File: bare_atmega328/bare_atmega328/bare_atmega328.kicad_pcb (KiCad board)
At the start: 2 copper layers, 43.7 x 56.4 mm, 21 parts, among them J1 22-23-2021, J2 22-23-2021, J3 640456-3, J4 22-23-2021, J5 Conn_01x14_Male, J6 Conn_01x14_Male, J7 22-23-2021, SW1 SW_Push, U1 ATMEGA328-PU, U2 NE555DR, Y1 Crystal

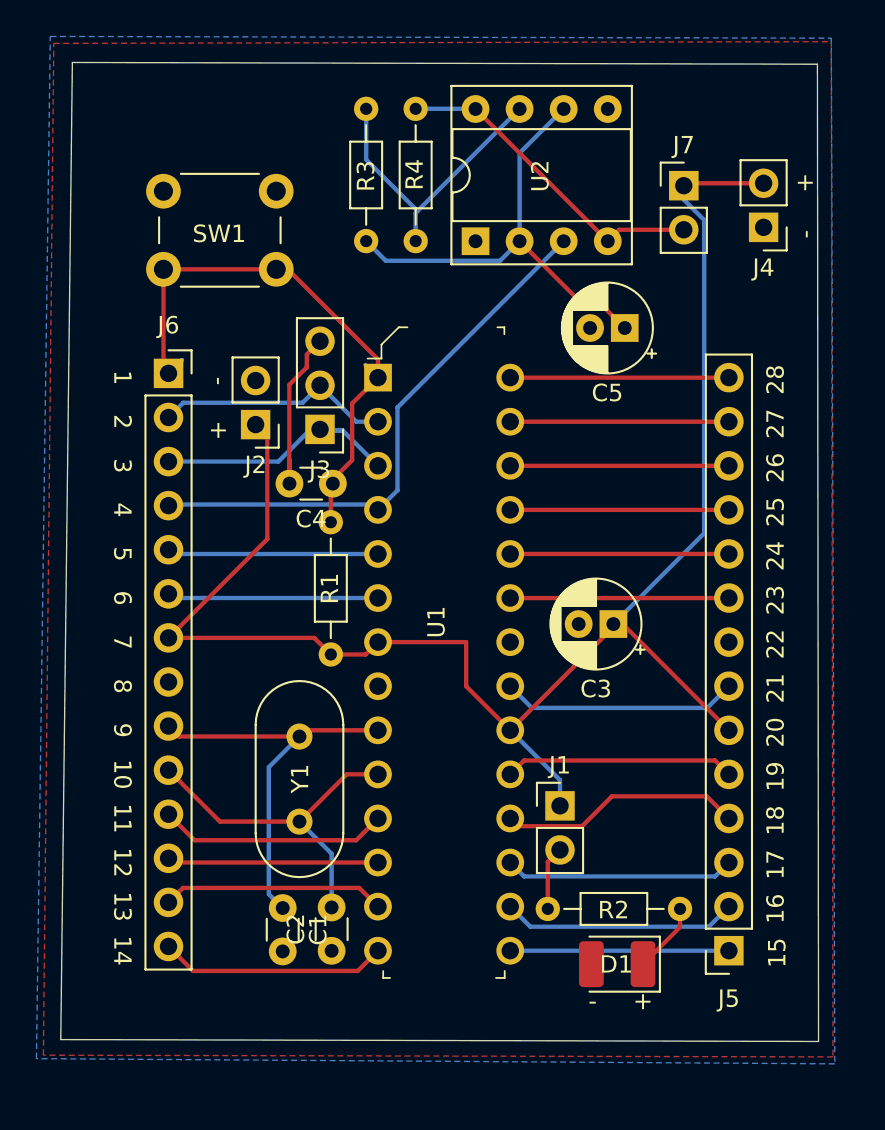
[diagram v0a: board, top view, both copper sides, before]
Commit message: Version v1.2 atmega328 + 555 timer
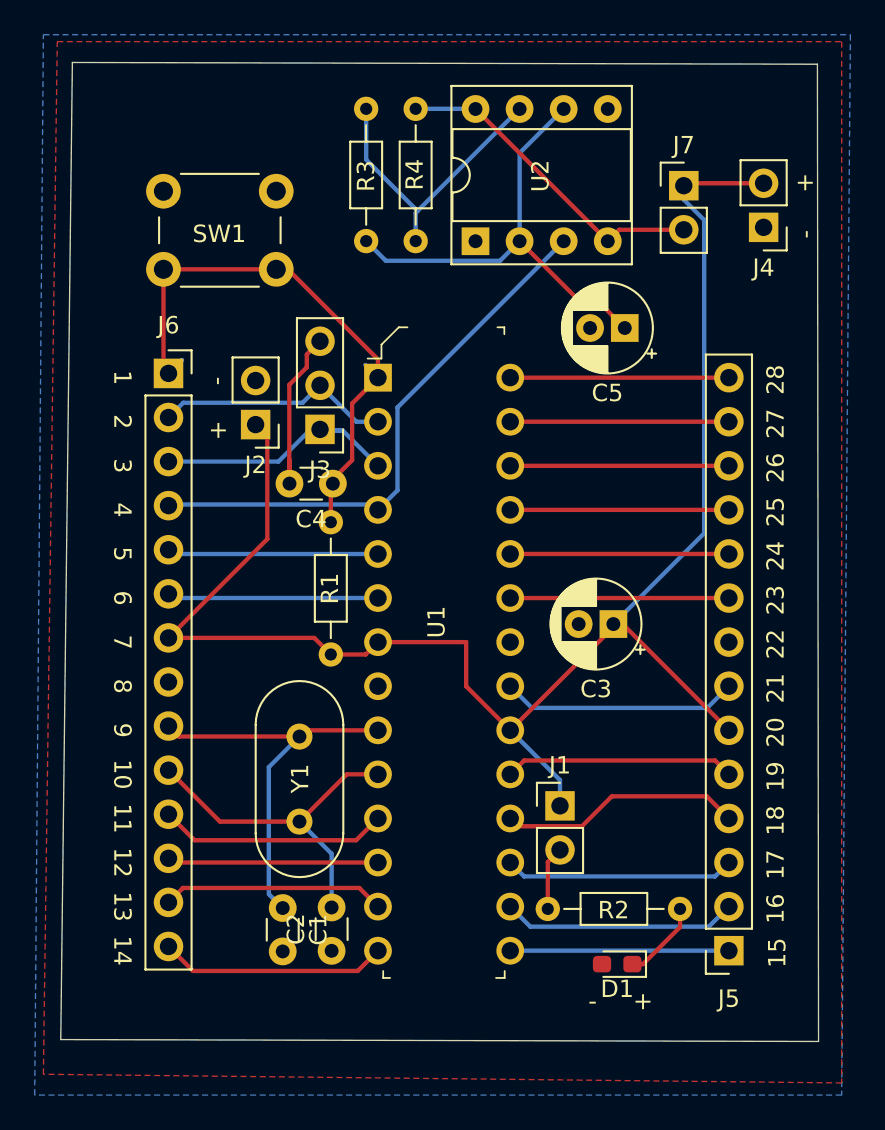
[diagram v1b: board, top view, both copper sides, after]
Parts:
- D1: footprint LED_SMD:LED_1210_3225Metric_Pad1.42x2.65mm_HandSolder -> LED_SMD:LED_0603_1608Metric_Pad1.05x0.95mm_HandSolder
- R2, R3: value R -> 220
- R4: value R -> 1M
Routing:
- net Net-(D1-Pad1): track 4.07 -> 4.68 mm
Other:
- board text added: "555 on/off"
- board text added: "Atmega328 + 555 V 1.2"
- board text added: "FTDI"
- board text added: "Led on/off"
- board text added: "Power"
